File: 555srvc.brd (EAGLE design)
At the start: 23 x 8 mm, 10 parts, among them IC1 555

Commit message: added OHW logo
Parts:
- added U$5: (no value), ohw-logo:OSHW_6X100_NOTEXT
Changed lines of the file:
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@@
 <attribute name="VALUE" x="16.964" y="-0.435" size="0.8128" layer="27"/>
 </element>
+<element name="U$5" library="ohw-logo" package="OSHW_6X100_NOTEXT" value="" x="13.7" y="0.3" rot="MR0"/>
 </elements>
 <signals>

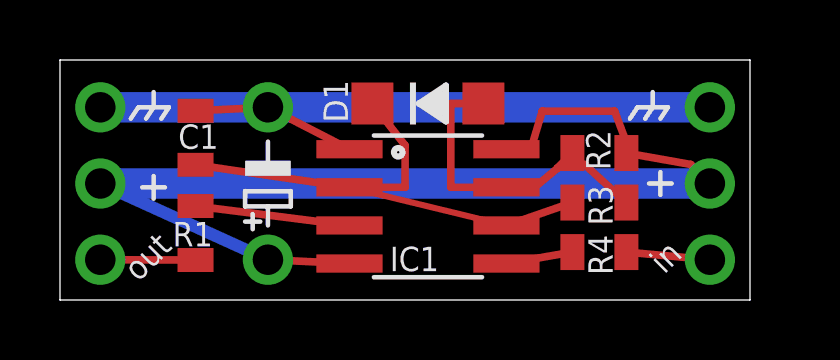
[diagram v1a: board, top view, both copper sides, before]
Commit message: sent to fab- panelized 4x10
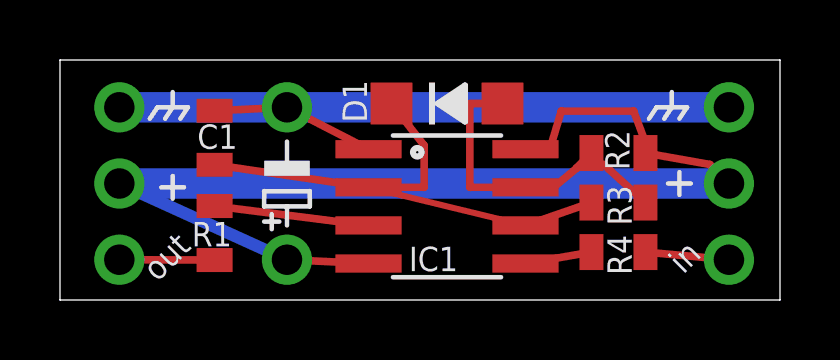
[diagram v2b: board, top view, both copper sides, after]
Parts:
- moved U$5 0.64 mm to (14.3, 0.30)
- moved JP2 0.64 mm to (1.98, 3.88)
- moved C1 0.63 mm to (5.15, 5.41)
- moved C2 0.63 mm to (7.57, 3.88)
- moved D1 0.63 mm to (12.9, 6.55)
- moved IC1 0.63 mm to (12.9, 3.12)
- moved R1 0.63 mm to (5.15, 2.23)
- moved JP3 0.63 mm to (22.3, 3.88)
- moved R2 0.63 mm to (18.6, 4.90)
- moved R3 0.63 mm to (18.6, 3.25)
- moved R4 0.63 mm to (18.6, 1.60)
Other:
- board size 23 x 8 mm -> 24 x 8 mm
